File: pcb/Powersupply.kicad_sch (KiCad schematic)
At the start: 39 parts, among them J3 Conn_02x04_Odd_Even, U4 TPS54325PWP.d, U5 TPS54294PWP

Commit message: pcb/layout: usbs and pds
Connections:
- net +1V0: now also J3.3 (Pin_3); no longer J3.7 (Pin_7)
- net +3V3: now also J3.7 (Pin_7); no longer J3.3 (Pin_3)
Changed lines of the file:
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@@
 	(symbol
 		(lib_id "power:+1V0")
-		(at 220.98 80.01 90)
+		(at 220.98 74.93 90)
 		(unit 1)
 		(body_style 1)
@@
 		(dnp no)
 		(property "Reference" "#PWR045"
-			(at 224.79 80.01 0)
+			(at 224.79 74.93 0)
 			(hide yes)
 			(show_name no)
@@
 		)
 		(property "Value" "+1V0"
-			(at 214.63 80.01 90)
+			(at 214.63 74.93 90)
 			(show_name no)
 			(do_not_autoplace no)
@@
 		)
 		(property "Footprint" ""
-			(at 220.98 80.01 0)
-			(hide yes)
-			(show_name no)
-			(do_not_autoplace no)
-			(effects
-				(font
-					(size 1.27 1.27)
-				)
-			)
-		)
-		(property "Datasheet" ""
-			(at 220.98 80.01 0)
+			(at 220.98 74.93 0)
+			(hide yes)
+			(show_name no)
+			(do_not_autoplace no)
+			(effects
+				(font
+					(size 1.27 1.27)
+				)
+			)
+		)
+		(property "Datasheet" ""
+			(at 220.98 74.93 0)
 			(hide yes)
 			(show_name no)
@@
 		)
 		(property "Description" "Power symbol creates a global label with name \"+1V0\""
-			(at 220.98 80.01 0)
+			(at 220.98 74.93 0)
 			(hide yes)
 			(show_name no)
@@
 	(symbol
 		(lib_id "power:+3.3V")
-		(at 220.98 74.93 90)
+		(at 220.98 80.01 90)
 		(unit 1)
 		(body_style 1)
@@
 		(fields_autoplaced yes)
 		(property "Reference" "#PWR043"
-			(at 224.79 74.93 0)
+			(at 224.79 80.01 0)
 			(hide yes)
 			(show_name no)
@@
 		)
 		(property "Value" "+3V3"
-			(at 217.17 74.9299 90)
+			(at 217.17 80.0099 90)
 			(show_name no)
 			(do_not_autoplace no)
@@
 		)
 		(property "Footprint" ""
-			(at 220.98 74.93 0)
-			(hide yes)
-			(show_name no)
-			(do_not_autoplace no)
-			(effects
-				(font
-					(size 1.27 1.27)
-				)
-			)
-		)
-		(property "Datasheet" ""
-			(at 220.98 74.93 0)
+			(at 220.98 80.01 0)
+			(hide yes)
+			(show_name no)
+			(do_not_autoplace no)
+			(effects
+				(font
+					(size 1.27 1.27)
+				)
+			)
+		)
+		(property "Datasheet" ""
+			(at 220.98 80.01 0)
 			(hide yes)
 			(show_name no)
@@
 		)
 		(property "Description" "Power symbol creates a global label with name \"+3.3V\""
-			(at 220.98 74.93 0)
-			(hide yes)
-			(show_name no)
+			(at 220.98 80.01 0)
+			(hide yes)
+			(show_name no)

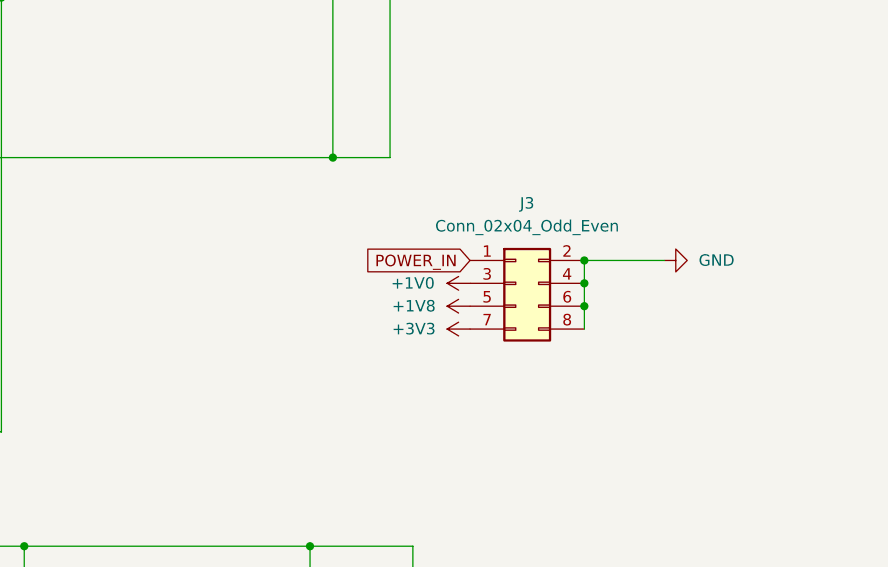
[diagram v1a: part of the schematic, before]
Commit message: changed footprint of J3
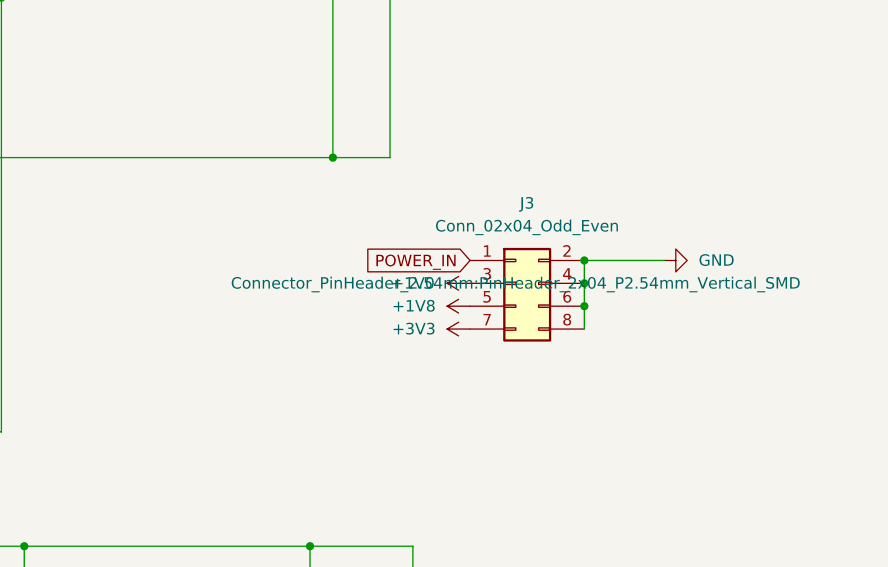
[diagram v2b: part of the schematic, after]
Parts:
- J3: footprint Connector_JST:JST_PUD_B08B-PUDSS_2x04_P2.00mm_Vertical -> Connector_PinHeader_2.54mm:PinHeader_2x04_P2.54mm_Vertical_SMD
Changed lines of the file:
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@@
 			)
 		)
-		(property "Footprint" "Connector_JST:JST_PUD_B08B-PUDSS_2x04_P2.00mm_Vertical"
+		(property "Footprint" "Connector_PinHeader_2.54mm:PinHeader_2x04_P2.54mm_Vertical_SMD"
 			(at 226.06 74.93 0)
-			(hide yes)
 			(show_name no)
 			(do_not_autoplace no)

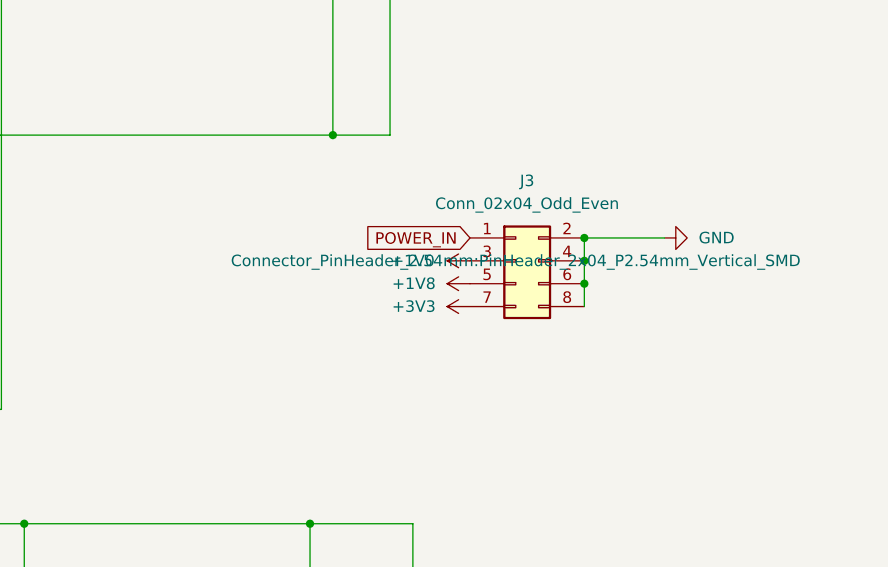
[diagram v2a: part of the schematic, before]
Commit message: added new jumper
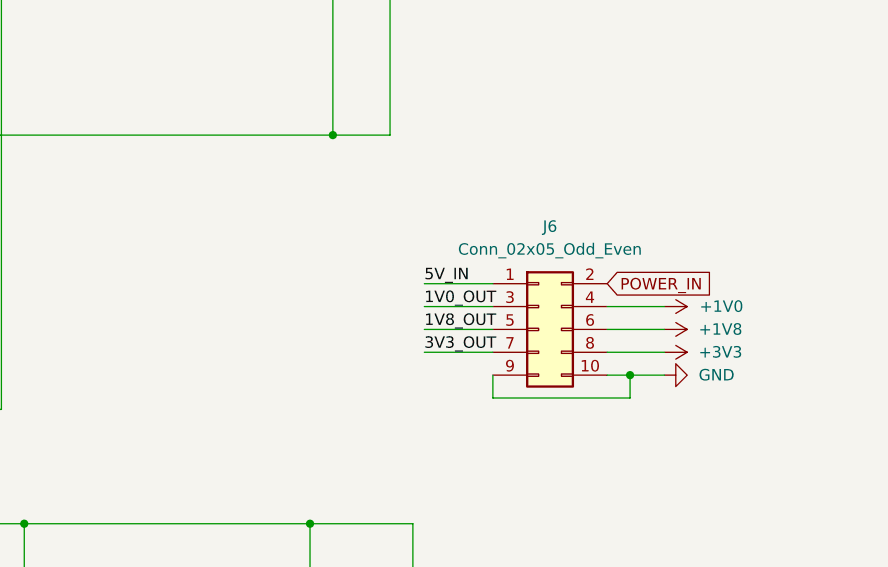
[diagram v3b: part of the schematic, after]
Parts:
- removed J3: Conn_02x04_Odd_Even, Connector_PinHeader_2.54mm:PinHeader_2x04_P2.54mm_Vertical_SMD, symbol Connector_Generic:Conn_02x04_Odd_Even
- added J6: Conn_02x05_Odd_Even, Connector_PinHeader_2.54mm:PinHeader_2x05_P2.54mm_Vertical_SMD, symbol Connector_Generic:Conn_02x05_Odd_Even
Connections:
- net +1V0: now also J6.4 (Pin_4)
- net +1V8: now also J6.6 (Pin_6)
- net +3V3: now also J6.8 (Pin_8)
- net GND: now also J6.10 (Pin_10), J6.9 (Pin_9)
- net POWER_IN: now also J6.2 (Pin_2)
- new net 1V0_OUT: J6.3 (Pin_3)
- new net 1V8_OUT: J6.5 (Pin_5)
- new net 3V3_OUT: J6.7 (Pin_7)
- new net 5V_IN: J6.1 (Pin_1)

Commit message: added new jumper complete
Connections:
- net +1V0: no longer C45.1, C46.1, L2.1, R36.1, U4.1 (VO)
- net +1V8: no longer C31.1, C32.1, L1.1, R31.1
- net +3V3: no longer C48.1, C49.1, L3.2, R40.1
- net 1V0_OUT: now also C45.1, C46.1, L2.1, R36.1, U4.1 (VO)
- net 1V8_OUT: now also C31.1, C32.1, L1.1, R31.1
- net 3V3_OUT: now also C48.1, C49.1, L3.2, R40.1

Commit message: new VGA model and footprint added
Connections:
- net 5V_IN: now also C33.1, C34.1, C35.1, C36.1, C37.1, C44.1, C47.1, U4.13 (VIN), U4.14 (VCC), U4.7 (EN), U5.1 (VIN1), U5.16 (VIN2)
- net POWER_IN: no longer C33.1, C34.1, C35.1, C36.1, C37.1, C44.1, C47.1, U4.13 (VIN), U4.14 (VCC), U4.7 (EN), U5.1 (VIN1), U5.16 (VIN2)

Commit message: fixed vga shield and tpsx94 footprint
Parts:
- U5: footprint TPS54294PWP:PWP16_2P31X2P46 -> Package_SO:HTSSOP-16-1EP_4.4x5mm_P0.65mm_EP3.4x5mm_Mask2.46x2.31mm_ThermalVias
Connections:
- net GND: now also U5.17 (EPAD); no longer U5.EPAD
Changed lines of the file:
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@@
 			)
 		)
-		(property "Footprint" "TPS54294PWP:PWP16_2P31X2P46"
+		(property "Footprint" "Package_SO:HTSSOP-16-1EP_4.4x5mm_P0.65mm_EP3.4x5mm_Mask2.46x2.31mm_ThermalVias"
 			(at 122.174 150.114 0)
 			(hide yes)
@@
 		(pin "12"
 		)
-		(pin "EPAD"
+		(pin "17"
 		)
 		(pin "16"

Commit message: added 3d model for powersupply
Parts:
- U5: footprint Package_SO:HTSSOP-16-1EP_4.4x5mm_P0.65mm_EP3.4x5mm_Mask2.46x2.31mm_ThermalVias -> Package_SO:HTSSOP-16-1EP_4.4x5mm_P0.65mm_EP3.4x5mm_Mask2.46x2.31mm
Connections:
- net 5V_IN: no longer C33.1, C34.1, C35.1, C36.1, C37.1, C44.1, C47.1, U4.13 (VIN), U4.14 (VCC), U4.7 (EN), U5.1 (VIN1), U5.16 (VIN2)
- net POWER_IN: now also C33.1, C34.1, C35.1, C36.1, C37.1, C44.1, C47.1, U4.13 (VIN), U4.14 (VCC), U4.7 (EN), U5.1 (VIN1), U5.16 (VIN2)
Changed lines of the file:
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@@
-		)
-	)
-	(label "5V_IN"
-		(at 50.8 33.02 180)
-		(effects
-			(font
-				(size 1.27 1.27)
-			)
-			(justify right bottom)
 		)
 	)
@@
 		)
 	)
+	(global_label "POWER_IN"
+		(shape input)
+		(at 50.8 33.02 180)
+		(effects
+			(font
+				(size 1.27 1.27)
+			)
+			(justify right)
+		)
+		(property "Intersheetrefs" "${INTERSHEET_REFS}"
+			(at 38.441 33.02 0)
+			(hide yes)
+			(show_name no)
+			(do_not_autoplace no)
+			(effects
+				(font
+					(size 1.27 1.27)
+				)
+				(justify right)
+			)
+		)
+		(property "Extra" "5V"
+			(at 39.116 32.766 0)
+			(show_name no)
+			(do_not_autoplace no)
+			(effects
+				(font
+					(size 1.27 1.27)
+					(color 15 0 171 1)
+				)
+				(justify right)
+			)
+		)
+	)
 	(symbol
 		(lib_id "Device:C")
@@
 			)
 		)
-		(property "Footprint" "Package_SO:HTSSOP-16-1EP_4.4x5mm_P0.65mm_EP3.4x5mm_Mask2.46x2.31mm_ThermalVias"
+		(property "Footprint" "Package_SO:HTSSOP-16-1EP_4.4x5mm_P0.65mm_EP3.4x5mm_Mask2.46x2.31mm"
 			(at 122.174 150.114 0)
 			(hide yes)

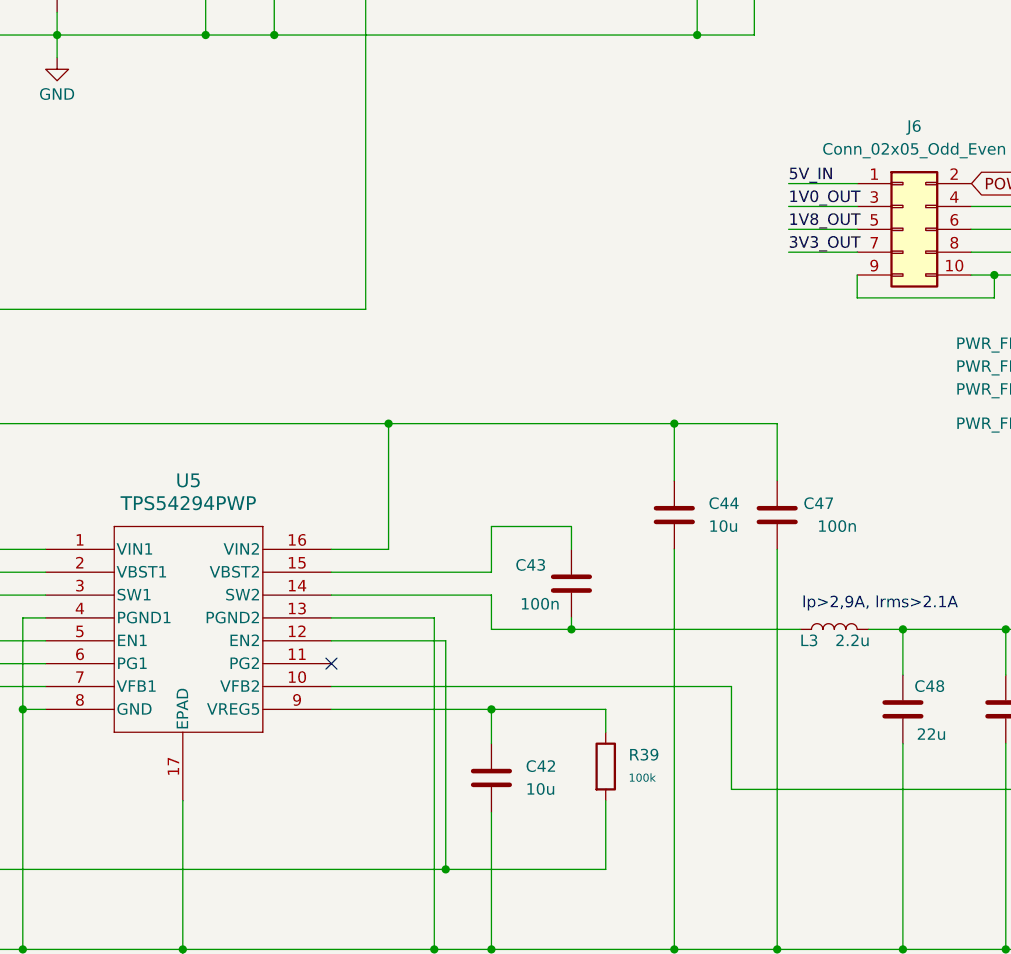
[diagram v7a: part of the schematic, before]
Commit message: fixed psd footprintgs and some routing
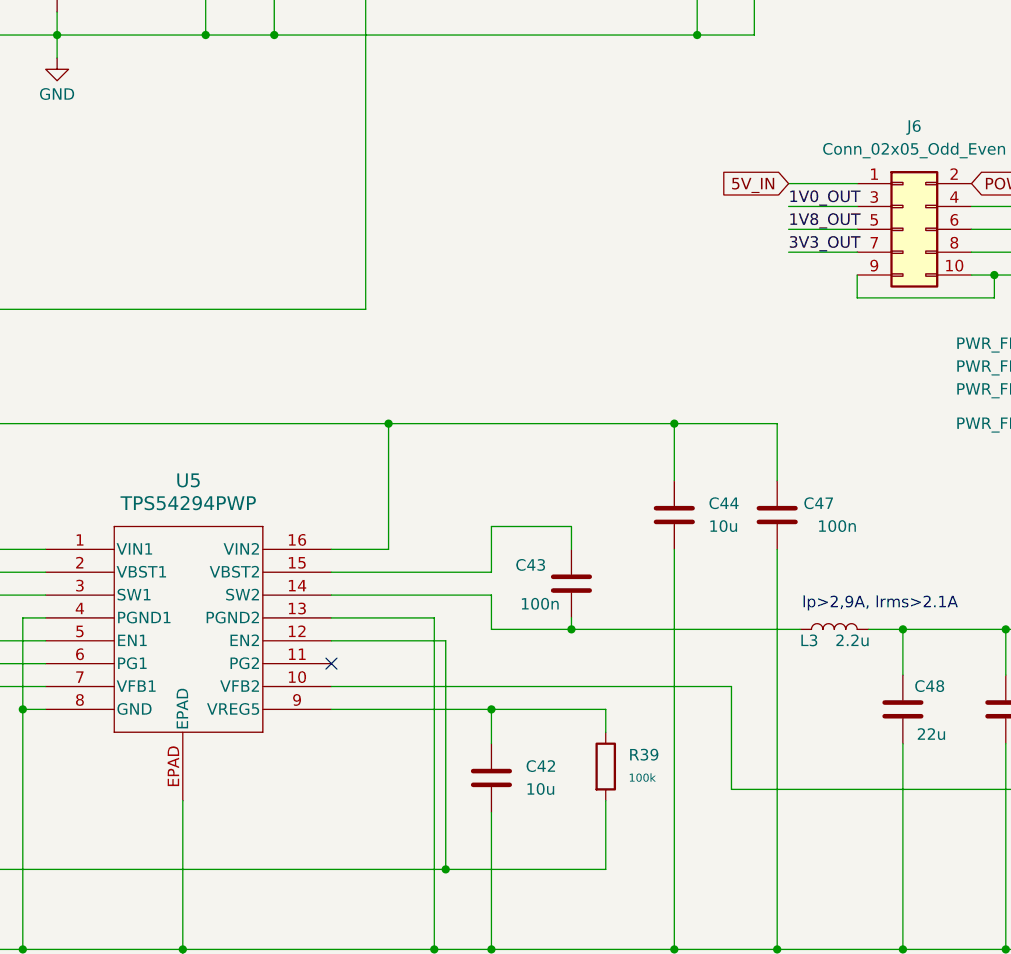
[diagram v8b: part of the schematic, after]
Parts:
- J6: footprint Connector_PinHeader_2.54mm:PinHeader_2x05_P2.54mm_Vertical_SMD -> Connector_PinHeader_2.54mm:PinHeader_2x05_P2.54mm_Vertical
- U5: footprint Package_SO:HTSSOP-16-1EP_4.4x5mm_P0.65mm_EP3.4x5mm_Mask2.46x2.31mm -> TPS54294PWP:PWP16_2P31X2P46
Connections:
- net GND: now also U5.EPAD; no longer U5.17 (EPAD)
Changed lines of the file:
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@@
 		)
 	)
-	(label "5V_IN"
-		(at 215.9 77.47 0)
-		(effects
-			(font
-				(size 1.27 1.27)
-			)
-			(justify left bottom)
-		)
-	)
 	(label "1V0_OUT"
 		(at 215.9 80.01 0)
@@
 		)
 	)
+	(global_label "5V_IN"
+		(shape input)
+		(at 215.9 77.47 180)
+		(fields_autoplaced yes)
+		(effects
+			(font
+				(size 1.27 1.27)
+			)
+			(justify right)
+		)
+		(property "Intersheetrefs" "${INTERSHEET_REFS}"
+			(at 207.7138 77.47 0)
+			(hide yes)
+			(show_name no)
+			(do_not_autoplace no)
+			(effects
+				(font
+					(size 1.27 1.27)
+				)
+				(justify right)
+			)
+		)
+	)
 	(global_label "POWER_IN"
 		(shape input)
@@
 			)
 		)
-		(property "Footprint" "Connector_PinHeader_2.54mm:PinHeader_2x05_P2.54mm_Vertical_SMD"
+		(property "Footprint" "Connector_PinHeader_2.54mm:PinHeader_2x05_P2.54mm_Vertical"
 			(at 228.6 82.55 0)
 			(hide yes)
@@
 			)
 		)
-		(property "Footprint" "Package_SO:HTSSOP-16-1EP_4.4x5mm_P0.65mm_EP3.4x5mm_Mask2.46x2.31mm"
+		(property "Footprint" "TPS54294PWP:PWP16_2P31X2P46"
 			(at 122.174 150.114 0)
 			(hide yes)
@@
 		(pin "12"
 		)
-		(pin "17"
+		(pin "EPAD"
 		)
 		(pin "16"
